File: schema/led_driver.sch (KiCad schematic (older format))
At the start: 1 part

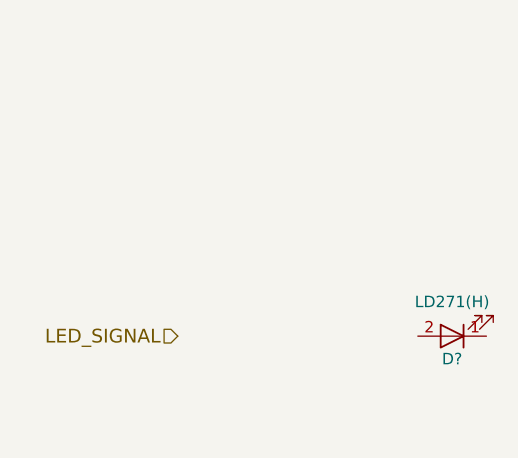
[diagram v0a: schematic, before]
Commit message: led driver MOS, correct opamp
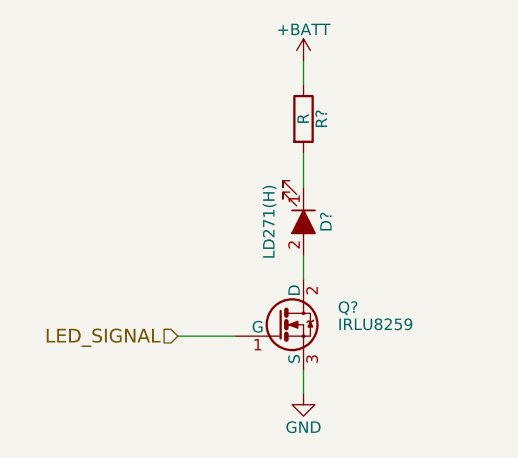
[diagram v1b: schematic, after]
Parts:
- removed D?: LD271(H), symbol LED-RESCUE-IRemote
- added D?: LD271(H), symbol LED_ALT
- added Q?: IRLU8259, TO_SOT_Packages_THT:TO-220_Neutral123_Vertical, symbol IRLB8721PBF
- added R?: R, symbol R
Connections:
- net LED_SIGNAL: now also Q?.1 (G)
- new net: D?.1 (K), R?.2
- new net: D?.2 (A), Q?.2 (D)
- new net +BATT: R?.1
- new net GND: Q?.3 (S)
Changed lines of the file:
@@
 LED_SIGNAL
 $Comp
-L LED-RESCUE-IRemote D?
-U 1 1 5910407B
-P 4400 2200
-F 0 "D?" H 4400 2300 50  0000 C CNN
-F 1 "LD271(H)" H 4400 2050 50  0000 C CNN
-F 2 "" H 4400 2200 50  0000 C CNN
-F 3 "" H 4400 2200 50  0000 C CNN
-	1    4400 2200
-	-1   0    0    1
+L LED_ALT D?
+U 1 1 59133BE7
+P 3750 1700
+F 0 "D?" H 3750 1800 50  0000 C CNN
+F 1 "LD271(H)" H 3750 1550 50  0000 C CNN
+F 2 "" H 3750 1700 50  0000 C CNN
+F 3 "" H 3750 1700 50  0000 C CNN
+	1    3750 1700
+	0    1    1    0
 $EndComp
+$Comp
+L IRLB8721PBF Q?
+U 1 1 59133C28
+P 3650 2150
+F 0 "Q?" H 3900 2225 50  0000 L CNN
+F 1 "IRLU8259" H 3900 2150 50  0000 L CNN
+F 2 "TO_SOT_Packages_THT:TO-220_Neutral123_Vertical" H 3900 2075 50  0001 L CIN
+F 3 "" H 3650 2150 50  0000 L CNN
+	1    3650 2150
+	1    0    0    -1
+$EndComp
+Wire Wire Line
+	3750 1850 3750 1950
+Wire Wire Line
+	3750 2350 3750 2450
+$Comp
+L GND #PWR?
+U 1 1 59133CA8
+P 3750 2450
+F 0 "#PWR?" H 3750 2200 50  0001 C CNN
+F 1 "GND" H 3750 2300 50  0000 C CNN
+F 2 "" H 3750 2450 50  0000 C CNN
+F 3 "" H 3750 2450 50  0000 C CNN
+	1    3750 2450
+	1    0    0    -1
+$EndComp
+Wire Wire Line
+	3450 2200 3200 2200
+Wire Wire Line
+	3750 1550 3750 1400
+$Comp
+L +BATT #PWR?
+U 1 1 59134055
+P 3750 1000
+F 0 "#PWR?" H 3750 850 50  0001 C CNN
+F 1 "+BATT" H 3750 1140 50  0000 C CNN
+F 2 "" H 3750 1000 50  0000 C CNN
+F 3 "" H 3750 1000 50  0000 C CNN
+	1    3750 1000
+	1    0    0    -1
+$EndComp
+$Comp
+L R R?
+U 1 1 59134208
+P 3750 1250
+F 0 "R?" V 3830 1250 50  0000 C CNN
+F 1 "R" V 3750 1250 50  0000 C CNN
+F 2 "" V 3680 1250 50  0000 C CNN
+F 3 "" H 3750 1250 50  0000 C CNN
+	1    3750 1250
+	1    0    0    -1
+$EndComp
+Wire Wire Line
+	3750 1000 3750 1100
 $EndSCHEMATC

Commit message: LED driver doc
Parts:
- R?: value R -> 1Ω
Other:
- note added: "V_forward = 1.9V\nI = 1A at 10% duty cycle"
- moved on the sheet: D?, Q?, R?
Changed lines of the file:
@@
 Comment4 ""
 $EndDescr
-Text HLabel 3200 2200 0    60   Input ~ 0
+Text HLabel 5750 4050 0    60   Input ~ 0
 LED_SIGNAL
 $Comp
 L LED_ALT D?
 U 1 1 59133BE7
-P 3750 1700
-F 0 "D?" H 3750 1800 50  0000 C CNN
-F 1 "LD271(H)" H 3750 1550 50  0000 C CNN
-F 2 "" H 3750 1700 50  0000 C CNN
-F 3 "" H 3750 1700 50  0000 C CNN
-	1    3750 1700
+P 6300 3550
+F 0 "D?" H 6300 3650 50  0000 C CNN
+F 1 "LD271(H)" H 6300 3400 50  0000 C CNN
+F 2 "" H 6300 3550 50  0000 C CNN
+F 3 "" H 6300 3550 50  0000 C CNN
+	1    6300 3550
 	0    1    1    0
 $EndComp
@@
 L IRLB8721PBF Q?
 U 1 1 59133C28
-P 3650 2150
-F 0 "Q?" H 3900 2225 50  0000 L CNN
-F 1 "IRLU8259" H 3900 2150 50  0000 L CNN
-F 2 "TO_SOT_Packages_THT:TO-220_Neutral123_Vertical" H 3900 2075 50  0001 L CIN
-F 3 "" H 3650 2150 50  0000 L CNN
-	1    3650 2150
+P 6200 4000
+F 0 "Q?" H 6450 4075 50  0000 L CNN
+F 1 "IRLU8259" H 6450 4000 50  0000 L CNN
+F 2 "TO_SOT_Packages_THT:TO-220_Neutral123_Vertical" H 6450 3925 50  0001 L CIN
+F 3 "" H 6200 4000 50  0000 L CNN
+	1    6200 4000
 	1    0    0    -1
 $EndComp
 Wire Wire Line
-	3750 1850 3750 1950
+	6300 3700 6300 3800
 Wire Wire Line
-	3750 2350 3750 2450
+	6300 4200 6300 4300
 $Comp
 L GND #PWR?
 U 1 1 59133CA8
-P 3750 2450
-F 0 "#PWR?" H 3750 2200 50  0001 C CNN
-F 1 "GND" H 3750 2300 50  0000 C CNN
-F 2 "" H 3750 2450 50  0000 C CNN
-F 3 "" H 3750 2450 50  0000 C CNN
-	1    3750 2450
+P 6300 4300
+F 0 "#PWR?" H 6300 4050 50  0001 C CNN
+F 1 "GND" H 6300 4150 50  0000 C CNN
+F 2 "" H 6300 4300 50  0000 C CNN
+F 3 "" H 6300 4300 50  0000 C CNN
+	1    6300 4300
 	1    0    0    -1
 $EndComp
 Wire Wire Line
-	3450 2200 3200 2200
+	6000 4050 5750 4050
 Wire Wire Line
-	3750 1550 3750 1400
+	6300 3400 6300 3250
 $Comp
 L +BATT #PWR?
 U 1 1 59134055
-P 3750 1000
-F 0 "#PWR?" H 3750 850 50  0001 C CNN
-F 1 "+BATT" H 3750 1140 50  0000 C CNN
-F 2 "" H 3750 1000 50  0000 C CNN
-F 3 "" H 3750 1000 50  0000 C CNN
-	1    3750 1000
+P 6300 2850
+F 0 "#PWR?" H 6300 2700 50  0001 C CNN
+F 1 "+BATT" H 6300 2990 50  0000 C CNN
+F 2 "" H 6300 2850 50  0000 C CNN
+F 3 "" H 6300 2850 50  0000 C CNN
+	1    6300 2850
 	1    0    0    -1
 $EndComp
@@
 L R R?
 U 1 1 59134208
-P 3750 1250
-F 0 "R?" V 3830 1250 50  0000 C CNN
-F 1 "R" V 3750 1250 50  0000 C CNN
-F 2 "" V 3680 1250 50  0000 C CNN
-F 3 "" H 3750 1250 50  0000 C CNN
-	1    3750 1250
+P 6300 3100
+F 0 "R?" V 6380 3100 50  0000 C CNN
+F 1 "1Ω" V 6300 3100 50  0000 C CNN
+F 2 "" V 6230 3100 50  0000 C CNN
+F 3 "" H 6300 3100 50  0000 C CNN
+	1    6300 3100
 	1    0    0    -1
 $EndComp
 Wire Wire Line
-	3750 1000 3750 1100
+	6300 2850 6300 2950
+Text Notes 6550 3600 0    60   ~ 0
+V_forward = 1.9V\nI = 1A at 10% duty cycle
 $EndSCHEMATC

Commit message: some filter modif
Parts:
- added C?: 470uF, symbol CP
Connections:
- net +BATT: now also C?.1
- net GND: now also C?.2
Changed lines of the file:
@@
 Text Notes 6550 3600 0    60   ~ 0
 V_forward = 1.9V\nI = 1A at 10% duty cycle
+$Comp
+L CP C?
+U 1 1 5921AD9D
+P 5800 3200
+F 0 "C?" H 5825 3300 50  0000 L CNN
+F 1 "470uF" H 5825 3100 50  0000 L CNN
+F 2 "" H 5838 3050 50  0000 C CNN
+F 3 "" H 5800 3200 50  0000 C CNN
+	1    5800 3200
+	1    0    0    -1
+$EndComp
+$Comp
+L GND #PWR?
+U 1 1 5921AE34
+P 5800 3350
+F 0 "#PWR?" H 5800 3100 50  0001 C CNN
+F 1 "GND" H 5800 3200 50  0000 C CNN
+F 2 "" H 5800 3350 50  0000 C CNN
+F 3 "" H 5800 3350 50  0000 C CNN
+	1    5800 3350
+	1    0    0    -1
+$EndComp
+Wire Wire Line
+	6300 2950 5800 2950
+Connection ~ 6300 2950
+Wire Wire Line
+	5800 2950 5800 3050
 $EndSCHEMATC

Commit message: filter and comparator
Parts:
- gave numbers to parts that had none: 4
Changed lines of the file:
@@
 LIBS:contrib
 LIBS:valves
+LIBS:custom
 LIBS:IRemote-cache
 EELAYER 25 0
@@
 LED_SIGNAL
 $Comp
-L LED_ALT D?
+L LED_ALT D1
 U 1 1 59133BE7
 P 6300 3550
-F 0 "D?" H 6300 3650 50  0000 C CNN
+F 0 "D1" H 6300 3650 50  0000 C CNN
 F 1 "LD271(H)" H 6300 3400 50  0000 C CNN
 F 2 "" H 6300 3550 50  0000 C CNN
@@
 $EndComp
 $Comp
-L IRLB8721PBF Q?
+L IRLB8721PBF Q2
 U 1 1 59133C28
 P 6200 4000
-F 0 "Q?" H 6450 4075 50  0000 L CNN
+F 0 "Q2" H 6450 4075 50  0000 L CNN
 F 1 "IRLU8259" H 6450 4000 50  0000 L CNN
 F 2 "TO_SOT_Packages_THT:TO-220_Neutral123_Vertical" H 6450 3925 50  0001 L CIN
@@
 	6300 4200 6300 4300
 $Comp
-L GND #PWR?
+L GND #PWR13
 U 1 1 59133CA8
 P 6300 4300
-F 0 "#PWR?" H 6300 4050 50  0001 C CNN
+F 0 "#PWR13" H 6300 4050 50  0001 C CNN
 F 1 "GND" H 6300 4150 50  0000 C CNN
 F 2 "" H 6300 4300 50  0000 C CNN
@@
 	6300 3400 6300 3250
 $Comp
-L +BATT #PWR?
+L +BATT #PWR12
 U 1 1 59134055
 P 6300 2850
-F 0 "#PWR?" H 6300 2700 50  0001 C CNN
+F 0 "#PWR12" H 6300 2700 50  0001 C CNN
 F 1 "+BATT" H 6300 2990 50  0000 C CNN
 F 2 "" H 6300 2850 50  0000 C CNN
@@
 $EndComp
 $Comp
-L R R?
+L R R14
 U 1 1 59134208
 P 6300 3100
-F 0 "R?" V 6380 3100 50  0000 C CNN
+F 0 "R14" V 6380 3100 50  0000 C CNN
 F 1 "1Ω" V 6300 3100 50  0000 C CNN
 F 2 "" V 6230 3100 50  0000 C CNN
@@
 V_forward = 1.9V\nI = 1A at 10% duty cycle
 $Comp
-L CP C?
+L CP C7
 U 1 1 5921AD9D
 P 5800 3200
-F 0 "C?" H 5825 3300 50  0000 L CNN
+F 0 "C7" H 5825 3300 50  0000 L CNN
 F 1 "470uF" H 5825 3100 50  0000 L CNN
 F 2 "" H 5838 3050 50  0000 C CNN
@@
 $EndComp
 $Comp
-L GND #PWR?
+L GND #PWR11
 U 1 1 5921AE34
 P 5800 3350
-F 0 "#PWR?" H 5800 3100 50  0001 C CNN
+F 0 "#PWR11" H 5800 3100 50  0001 C CNN
 F 1 "GND" H 5800 3200 50  0000 C CNN
 F 2 "" H 5800 3350 50  0000 C CNN
